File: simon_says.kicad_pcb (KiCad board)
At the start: 2 copper layers, 97 x 60 mm, 24 parts, among them SW1 SW_Push_LED, SW2 SW_Push_LED, SW3 SW_Push_LED, SW4 SW_Push_LED, SW5 SW_Push, U1 ATtiny25-20P

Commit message: Added order number placeholder
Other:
- board text added: "JLCJLCJLCJLC"
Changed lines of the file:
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@@
   (gr_line (start 147 55) (end 147 67)
     (stroke (width 0.1) (type default)) (layer "Edge.Cuts"))
+  (gr_text "JLCJLCJLCJLC" (at 98.575 105.775) (layer "B.SilkS")
+    (effects (font (size 1.5 1.5) (thickness 0.2)) (justify mirror))
+  )
   (gr_text "CR2450" (at 122.43 54.84) (layer "B.SilkS")
     (effects (font (size 1.5 1.5) (thickness 0.3) bold) (justify mirror))

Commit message: Updated front decorations
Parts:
- moved D3 35.1 mm to (50.1, 74.1)
- moved D2 35.1 mm to (97.1, 74.1)
- moved R1 35.1 mm to (106.1, 56.7)
- moved R2 35.1 mm to (43.1, 54.2)
- moved ? 35.1 mm to (58.1, 37.2)
- moved D1 35.1 mm to (50.1, 36.2)
- moved R3 35.1 mm to (41.0, 56.3)
- moved REF** 35.1 mm to (30.1, 30.2)
- moved REF** 35.1 mm to (30.1, 80.2)
- moved SW1 35.1 mm to (40.1, 40.2)
- moved SW2 35.1 mm to (40.1, 70.2)
- moved ? 35.1 mm to (89.1, 37.2)
- moved C1 35.1 mm to (73.6, 60.9)
- moved D4 35.1 mm to (97.1, 36.2)
- moved LS1 35.1 mm to (73.6, 53.2)
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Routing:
- net +BATT: track 83.0 -> 39.1 mm
- net PB2: track 229.4 -> 229.9 mm
- added copper zone on F.Cu, net +BATT

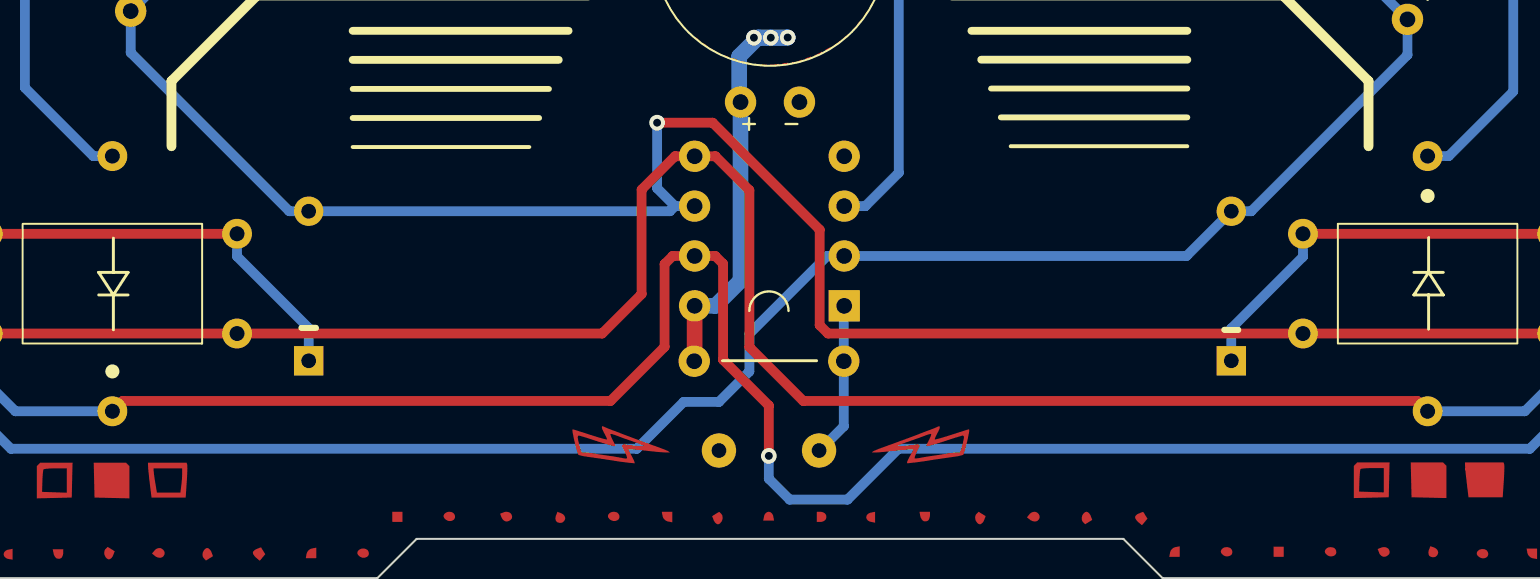
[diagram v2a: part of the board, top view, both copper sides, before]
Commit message: Fixed traces' clearance
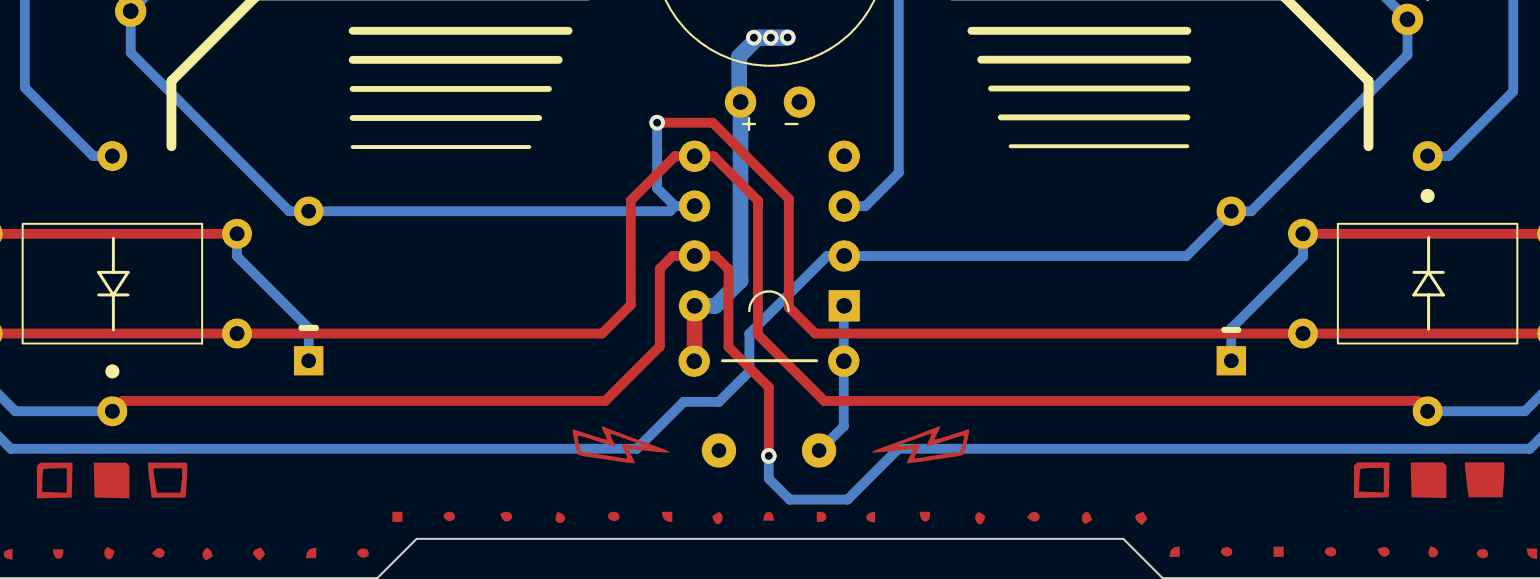
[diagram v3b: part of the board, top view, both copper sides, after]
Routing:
- net PB0: track 163.1 -> 162.4 mm
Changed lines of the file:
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@@
   (segment (start 100.764349 42.718522) (end 98.264349 42.718522) (width 0.5) (layer "B.Cu") (net 5))
   (segment (start 67.864349 61.978522) (end 70.694349 61.978522) (width 0.5) (layer "F.Cu") (net 6))
+  (segment (start 75.918522 72.718522) (end 100.764349 72.718522) (width 0.5) (layer "F.Cu") (net 6))
+  (segment (start 74.575 71.375) (end 75.918522 72.718522) (width 0.5) (layer "F.Cu") (net 6))
   (segment (start 113.464349 72.718522) (end 100.764349 72.718522) (width 0.5) (layer "F.Cu") (net 6))
-  (segment (start 76.144349 67.428522) (end 76.144349 72.294918) (width 0.5) (layer "F.Cu") (net 6))
-  (segment (start 70.694349 61.978522) (end 76.144349 67.428522) (width 0.5) (layer "F.Cu") (net 6))
-  (segment (start 76.144349 72.294918) (end 76.567953 72.718522) (width 0.5) (layer "F.Cu") (net 6))
-  (segment (start 76.567953 72.718522) (end 100.764349 72.718522) (width 0.5) (layer "F.Cu") (net 6))
+  (segment (start 70.694349 61.978522) (end 74.575 65.859173) (width 0.5) (layer "F.Cu") (net 6))
+  (segment (start 74.575 65.859173) (end 74.575 71.375) (width 0.5) (layer "F.Cu") (net 6))
   (via (at 67.864349 61.978522) (size 0.8) (drill 0.4) (layers "F.Cu" "B.Cu") (net 6))
   (segment (start 69.774349 66.228522) (end 68.774349 66.228522) (width 0.5) (layer "B.Cu") (net 6))
@@
   (segment (start 67.864349 61.978522) (end 67.864349 65.318522) (width 0.5) (layer "B.Cu") (net 6))
   (segment (start 67.864349 65.318522) (end 68.774349 66.228522) (width 0.5) (layer "B.Cu") (net 6))
-  (segment (start 71.224349 74.058522) (end 71.224349 69.168522) (width 0.5) (layer "F.Cu") (net 7))
+  (segment (start 73.554349 78.953522) (end 73.554349 75.454349) (width 0.5) (layer "F.Cu") (net 7))
+  (segment (start 68.654349 68.768522) (end 68 69.422871) (width 0.5) (layer "F.Cu") (net 7))
+  (segment (start 71.5 73.4) (end 71.5 69.444173) (width 0.5) (layer "F.Cu") (net 7))
+  (segment (start 68 73.375) (end 65.221478 76.153522) (width 0.5) (layer "F.Cu") (net 7))
+  (segment (start 68 69.422871) (end 68 73.375) (width 0.5) (layer "F.Cu") (net 7))
+  (segment (start 71.5 69.444173) (end 70.824349 68.768522) (width 0.5) (layer "F.Cu") (net 7))
+  (segment (start 40.114349 33.678522) (end 40.114349 37.638522) (width 0.5) (layer "F.Cu") (net 7))
+  (segment (start 33.764349 37.638522) (end 40.114349 37.638522) (width 0.5) (layer "F.Cu") (net 7))
+  (segment (start 65.221478 76.153522) (end 40.639349 76.153522) (width 0.5) (layer "F.Cu") (net 7))
+  (segment (start 73.554349 75.454349) (end 71.5 73.4) (width 0.5) (layer "F.Cu") (net 7))
   (segment (start 70.824349 68.768522) (end 69.774349 68.768522) (width 0.5) (layer "F.Cu") (net 7))
+  (segment (start 40.114349 37.638522) (end 46.464349 37.638522) (width 0.5) (layer "F.Cu") (net 7))
   (segment (start 69.774349 68.768522) (end 68.654349 68.768522) (width 0.5) (layer "F.Cu") (net 7))
-  (segment (start 65.489349 76.153522) (end 40.639349 76.153522) (width 0.5) (layer "F.Cu") (net 7))
-  (segment (start 68.244349 69.178522) (end 68.244349 73.398522) (width 0.5) (layer "F.Cu") (net 7))
-  (segment (start 40.114349 33.678522) (end 40.114349 37.638522) (width 0.5) (layer "F.Cu") (net 7))
-  (segment (start 73.554349 76.388522) (end 71.224349 74.058522) (width 0.5) (layer "F.Cu") (net 7))
-  (segment (start 33.764349 37.638522) (end 40.114349 37.638522) (width 0.5) (layer "F.Cu") (net 7))
   (segment (start 40.639349 76.153522) (end 40.114349 76.678522) (width 0.5) (layer "F.Cu") (net 7))
-  (segment (start 71.224349 69.168522) (end 70.824349 68.768522) (width 0.5) (layer "F.Cu") (net 7))
-  (segment (start 40.114349 37.638522) (end 46.464349 37.638522) (width 0.5) (layer "F.Cu") (net 7))
-  (segment (start 73.554349 78.953522) (end 73.554349 76.388522) (width 0.5) (layer "F.Cu") (net 7))
-  (segment (start 68.244349 73.398522) (end 65.489349 76.153522) (width 0.5) (layer "F.Cu") (net 7))
-  (segment (start 68.654349 68.768522) (end 68.244349 69.178522) (width 0.5) (layer "F.Cu") (net 7))
   (via (at 73.554349 78.953522) (size 0.8) (drill 0.4) (layers "F.Cu" "B.Cu") (net 7))
   (segment (start 74.614349 81.178522) (end 77.564349 81.178522) (width 0.5) (layer "B.Cu") (net 7))
@@
   (segment (start 108.170272 49.234445) (end 109.383426 49.234445) (width 0.5) (layer "B.Cu") (net 12))
   (segment (start 107.114349 46.678522) (end 107.114349 48.178522) (width 0.5) (layer "B.Cu") (net 12))
+  (segment (start 68.774349 63.688522) (end 69.774349 63.688522) (width 0.5) (layer "F.Cu") (net 13))
+  (segment (start 73 65.95) (end 73 72.775) (width 0.5) (layer "F.Cu") (net 13))
+  (segment (start 46.464349 72.718522) (end 65.064349 72.718522) (width 0.5) (layer "F.Cu") (net 13))
   (segment (start 113.464349 37.638522) (end 107.184349 37.638522) (width 0.5) (layer "F.Cu") (net 13))
-  (segment (start 69.774349 63.688522) (end 70.834349 63.688522) (width 0.5) (layer "F.Cu") (net 13))
   (segment (start 107.114349 37.568522) (end 107.184349 37.638522) (width 0.5) (layer "F.Cu") (net 13))
-  (segment (start 75.309349 76.153522) (end 106.589349 76.153522) (width 0.5) (layer "F.Cu") (net 13))
   (segment (start 107.184349 37.638522) (end 100.764349 37.638522) (width 0.5) (layer "F.Cu") (net 13))
-  (segment (start 72.564349 65.418522) (end 72.564349 73.408522) (width 0.5) (layer "F.Cu") (net 13))
-  (segment (start 72.564349 73.408522) (end 75.309349 76.153522) (width 0.5) (layer "F.Cu") (net 13))
-  (segment (start 46.464349 72.718522) (end 65.064349 72.718522) (width 0.5) (layer "F.Cu") (net 13))
-  (segment (start 67.074349 65.388522) (end 68.774349 63.688522) (width 0.5) (layer "F.Cu") (net 13))
+  (segment (start 65.064349 72.718522) (end 66.525 71.257871) (width 0.5) (layer "F.Cu") (net 13))
+  (segment (start 66.525 65.937871) (end 68.774349 63.688522) (width 0.5) (layer "F.Cu") (net 13))
+  (segment (start 66.525 71.257871) (end 66.525 65.937871) (width 0.5) (layer "F.Cu") (net 13))
+  (segment (start 106.589349 76.153522) (end 107.114349 76.678522) (width 0.5) (layer "F.Cu") (net 13))
   (segment (start 107.114349 33.678522) (end 107.114349 37.568522) (width 0.5) (layer "F.Cu") (net 13))
-  (segment (start 67.074349 70.708522) (end 67.074349 65.388522) (width 0.5) (layer "F.Cu") (net 13))
-  (segment (start 106.589349 76.153522) (end 107.114349 76.678522) (width 0.5) (layer "F.Cu") (net 13))
-  (segment (start 68.774349 63.688522) (end 69.774349 63.688522) (width 0.5) (layer "F.Cu") (net 13))
-  (segment (start 65.064349 72.718522) (end 67.074349 70.708522) (width 0.5) (layer "F.Cu") (net 13))
+  (segment (start 73 72.775) (end 76.378522 76.153522) (width 0.5) (layer "F.Cu") (net 13))
+  (segment (start 69.774349 63.688522) (end 70.738522 63.688522) (width 0.5) (layer "F.Cu") (net 13))
+  (segment (start 70.738522 63.688522) (end 73 65.95) (width 0.5) (layer "F.Cu") (net 13))
   (segment (start 46.464349 72.718522) (end 33.764349 72.718522) (width 0.5) (layer "F.Cu") (net 13))
-  (segment (start 70.834349 63.688522) (end 72.564349 65.418522) (width 0.5) (layer "F.Cu") (net 13))
+  (segment (start 76.378522 76.153522) (end 106.589349 76.153522) (width 0.5) (layer "F.Cu") (net 13))
   (segment (start 115.974349 37.628522) (end 115.974349 72.768522) (width 0.5) (layer "B.Cu") (net 13))
   (segment (start 115.974349 72.768522) (end 112.064349 76.678522) (width 0.5) (layer "B.Cu") (net 13))

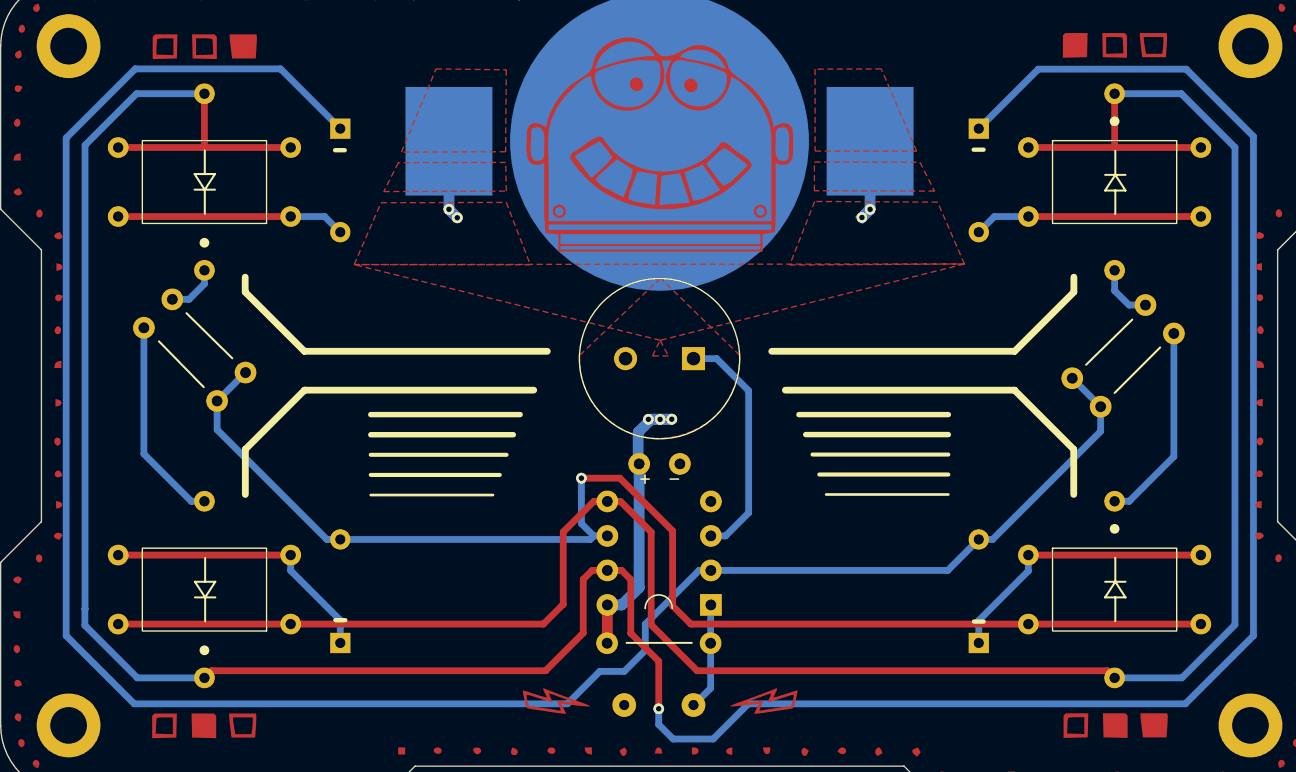
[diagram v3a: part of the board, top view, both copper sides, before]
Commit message: Small fixes on pads and vias
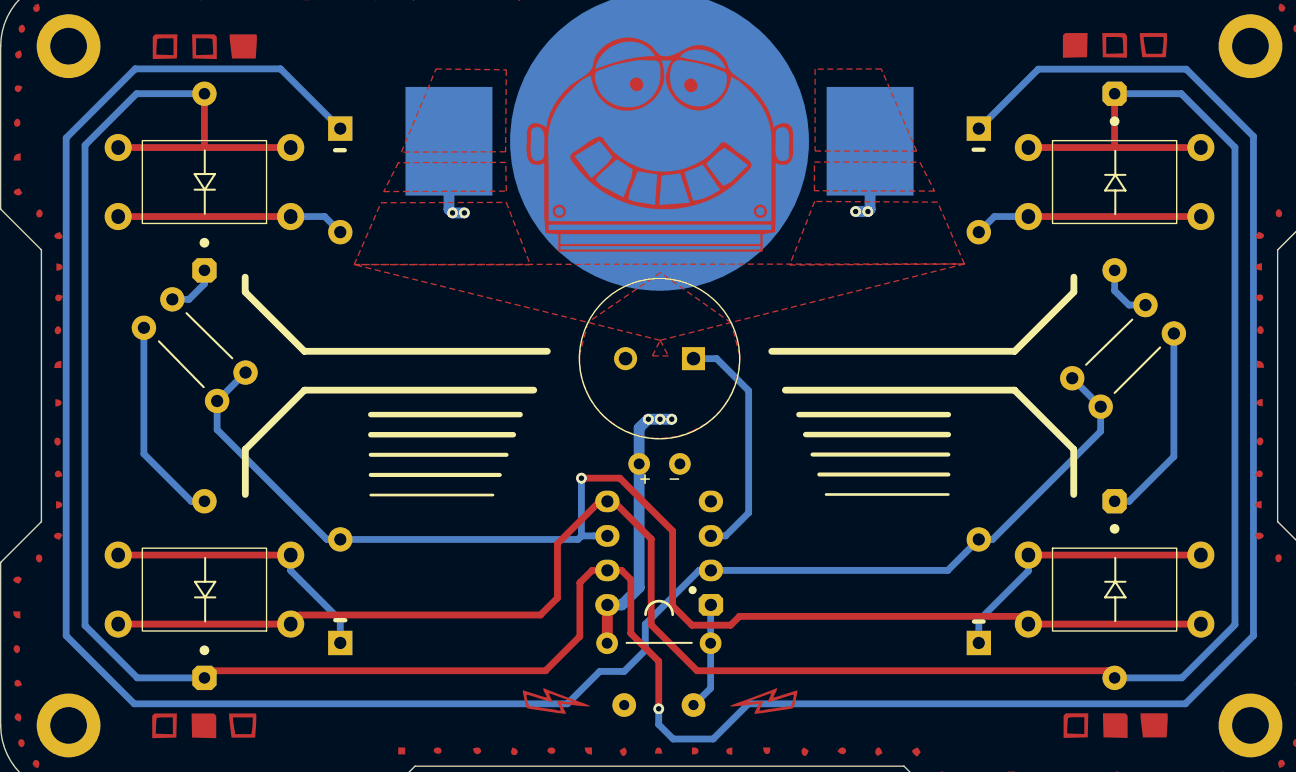
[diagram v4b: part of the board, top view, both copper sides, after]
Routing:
- net PB0: track 162.4 -> 161.3 mm
- net +BATT: track 39.1 -> 38.1 mm

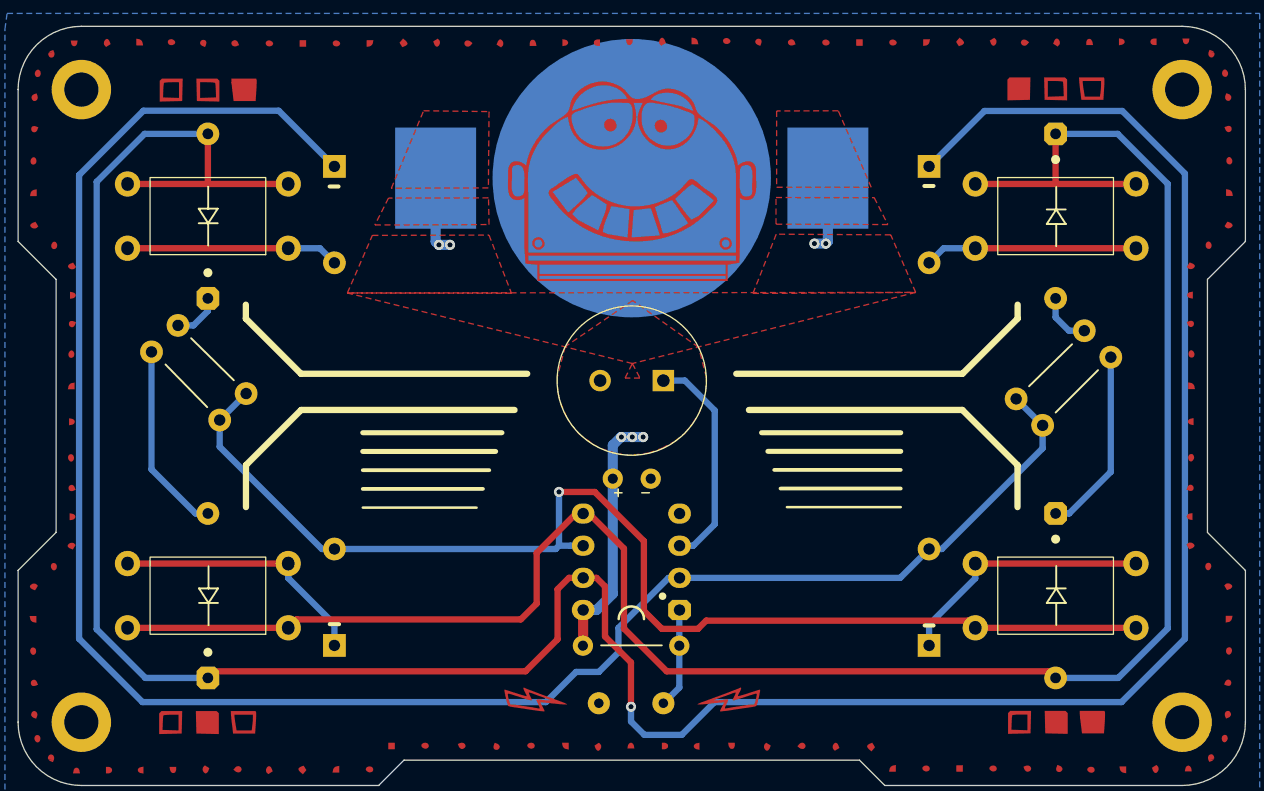
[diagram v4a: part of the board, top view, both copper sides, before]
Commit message: Further enlarge hole size on pads
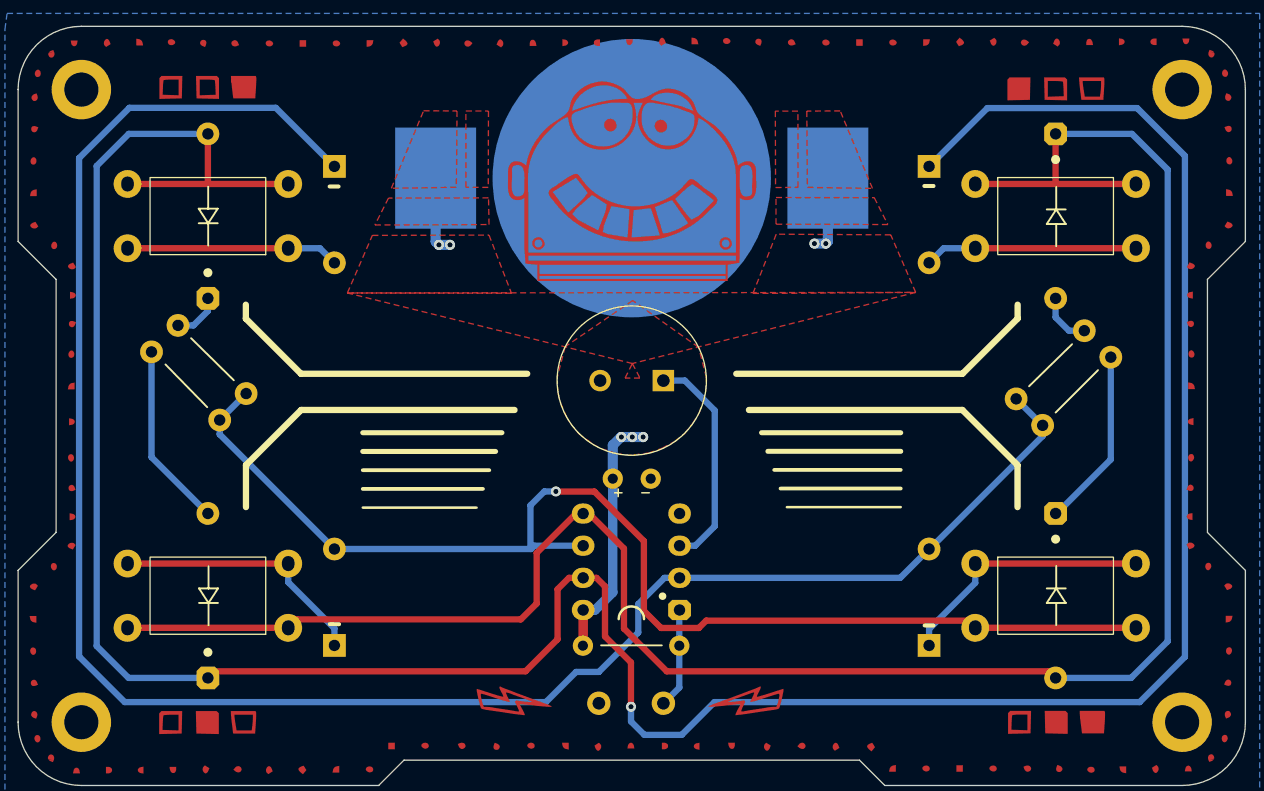
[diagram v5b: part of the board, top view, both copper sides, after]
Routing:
- net PB2: track 229.8 -> 233.1 mm
- net PB3: track 153.2 -> 154.6 mm
- net PB1: track 95.3 -> 96.6 mm
- net PB0: track 161.3 -> 162.6 mm
- net Net-(SW3-K): track 14.8 -> 14.2 mm
- net Net-(SW2-A): track 15.2 -> 14.6 mm
